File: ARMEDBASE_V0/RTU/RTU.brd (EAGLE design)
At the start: 160 x 100 mm, 25 parts, among them IC1 REG1117, IC2 MEGA8-P, Q1 20Mhz, Q2 2N3904

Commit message: 7805
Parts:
- moved S2 20.5 mm to (5.08, 76.2)
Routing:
- net N$24: track 41.4 -> 74.2 mm, vias 1 -> 0
- net VCC12V: track 41.4 -> 11.7 mm
- net VCC5V: track 129.9 -> 158.8 mm, vias 1 -> 2
- net GND: track 156.7 -> 173.1 mm
- net N$13: track 29.2 -> 16.4 mm
- net N$8: track 46.5 -> 51.1 mm, vias 1 -> 0
- net N$4: track 25.5 -> 24.1 mm
- net RX: track 53.8 -> 53.1 mm

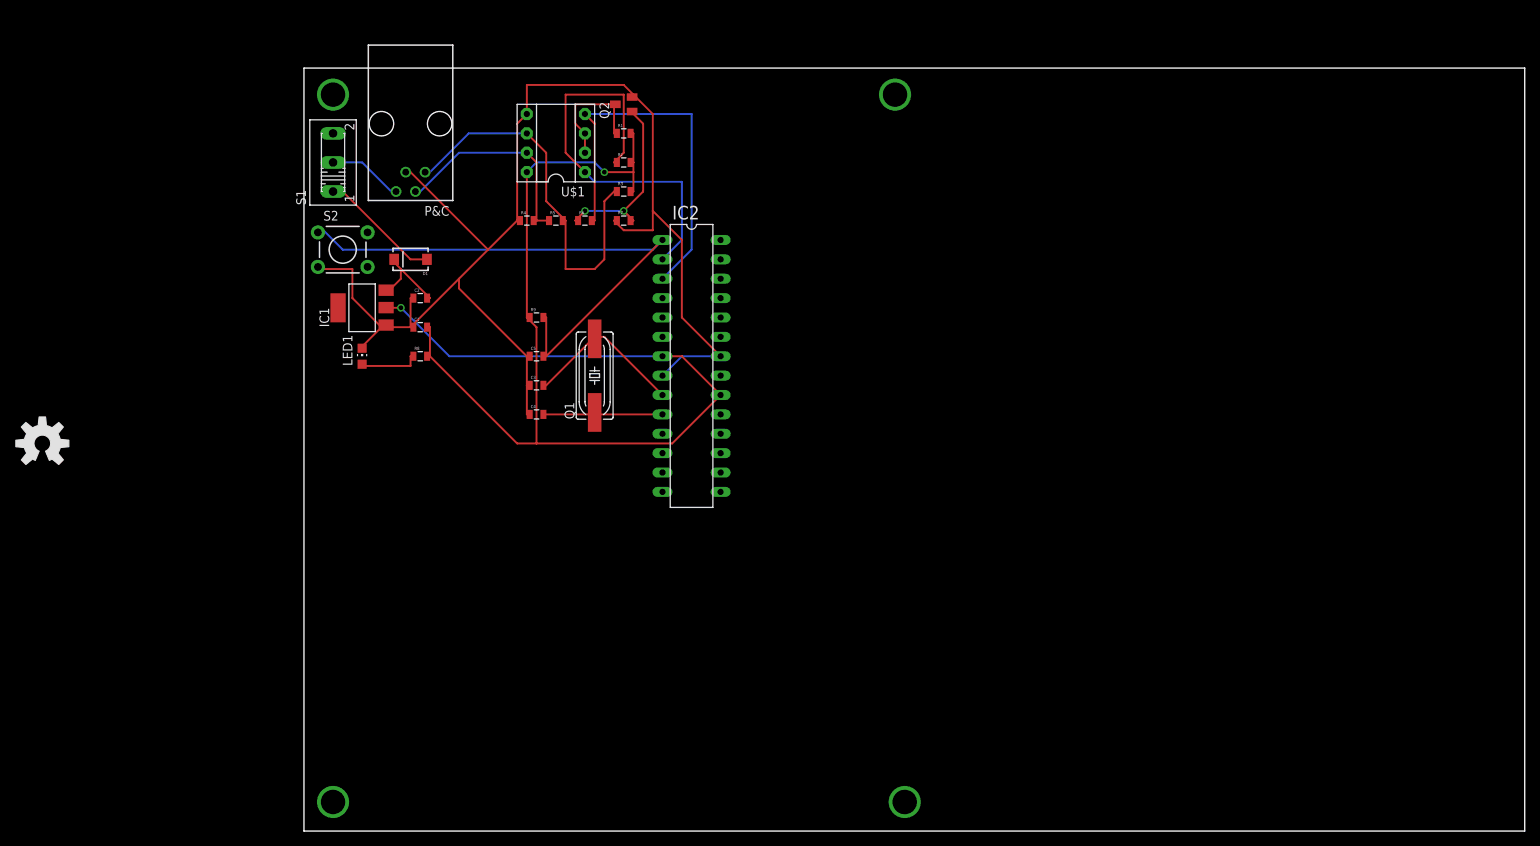
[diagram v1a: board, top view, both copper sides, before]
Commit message: modbus in-out
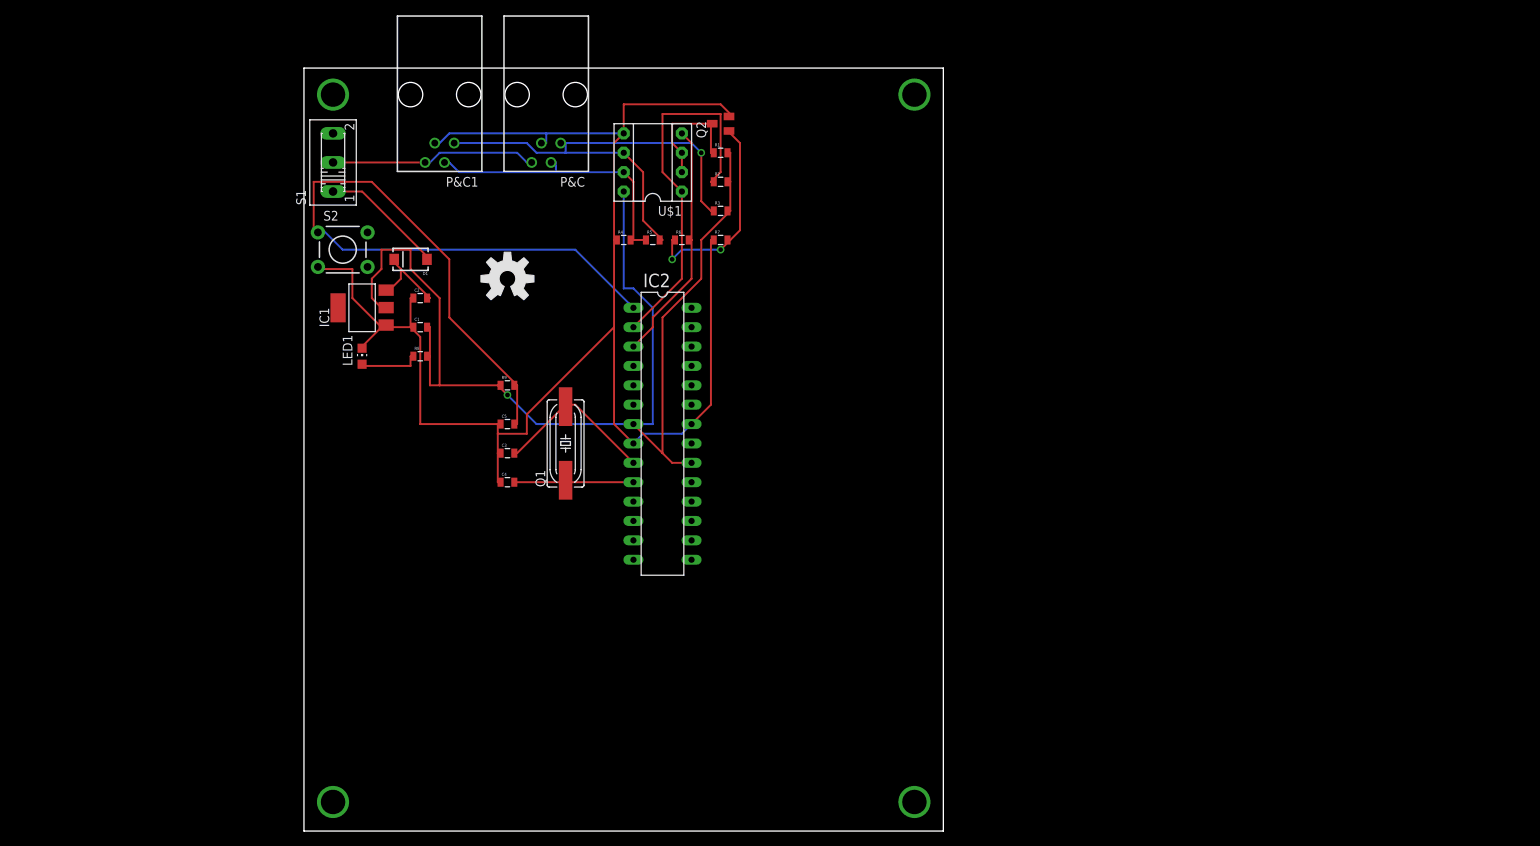
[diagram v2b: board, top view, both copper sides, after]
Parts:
- added P&C1: 14867, con-4ucon:14867
- moved LOGO1 64.7 mm to (26.7, 72.4)
- moved P&C 18.2 mm to (31.8, 96.5)
- moved Q2 13.0 mm to (54.6, 92.7)
- moved R6 13.0 mm to (49.5, 77.5)
- moved R7 13.0 mm to (54.6, 77.5)
- moved R1 13.0 mm to (54.6, 88.9)
- moved R2 13.0 mm to (54.6, 85.1)
- moved R3 13.0 mm to (54.6, 81.3)
- moved R4 13.0 mm to (41.9, 77.5)
- moved R5 13.0 mm to (45.7, 77.5)
- moved U$1 13.0 mm to (45.7, 87.6)
- moved C3 9.67 mm to (26.7, 49.5)
- moved C4 9.67 mm to (26.7, 45.7)
- moved Q1 9.67 mm to (34.3, 50.8)
- moved R9 9.67 mm to (26.7, 58.4)
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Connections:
- net GND: now also P&C1.3
- net N$7: now also P&C1.2
- net N$8: now also P&C1.1
- net VCC: now also P&C1.4
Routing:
- net GND: track 173.1 -> 203.4 mm
- net N$24: track 74.2 -> 100.6 mm
- net TX: track 52.0 -> 32.0 mm
- net VCC: track 9.83 -> 27.1 mm
- net N$8: track 51.1 -> 65.4 mm, vias 0 -> 1
- net N$7: track 28.1 -> 37.4 mm
- net RX: track 53.1 -> 49.0 mm
- net N$4: track 24.1 -> 27.3 mm
- net VCC5V: track 158.8 -> 159.2 mm, vias 2 -> 1
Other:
- board size 160 x 100 mm -> 83.8 x 100 mm

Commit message: arg
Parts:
- moved R9 13.1 mm to (20.3, 69.8)
- moved LED1 10.2 mm to (17.8, 62.2), turned to 90 degrees
- moved R8 6.35 mm to (20.3, 66.0), turned to 180 degrees
- moved Q2 2.84 mm to (55.9, 95.2)
- moved R4 2.84 mm to (43.2, 80.0)
- moved R5 2.84 mm to (47.0, 80.0)
- moved R7 2.84 mm to (55.9, 80.0)
- moved U$1 2.84 mm to (47.0, 90.2)
- moved R6 2.84 mm to (50.8, 80.0)
- moved R1 2.84 mm to (55.9, 91.4)
- moved R2 2.84 mm to (55.9, 87.6)
- moved R3 2.84 mm to (55.9, 83.8)
- moved D1 2.54 mm to (16.5, 74.9)
- moved S2 1.80 mm to (6.35, 77.5)
- moved S1 1.27 mm to (2.54, 87.6)
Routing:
- net N$24: track 100.6 -> 72.4 mm, vias 0 -> 1
- net GND: track 203.4 -> 218.3 mm
- net VCC5V: track 159.2 -> 148.5 mm, vias 1 -> 0
- net N$8: track 65.4 -> 56.4 mm
- net N$13: track 16.8 -> 20.6 mm
- net TX: track 32.0 -> 35.1 mm
- net RX: track 49.0 -> 52.1 mm
- net N$11: track 8.21 -> 5.45 mm
- net VCC: track 27.1 -> 28.4 mm
- net N$4: track 27.3 -> 26.6 mm
- net VCC12V: track 11.7 -> 11.2 mm

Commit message: rtu org
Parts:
- moved R3 33.4 mm to (22.9, 78.7), turned to 180 degrees
- moved R4 25.5 mm to (17.8, 82.5)
- moved R5 24.3 mm to (22.9, 82.5)
- moved R7 19.8 mm to (41.9, 94.0), turned to 90 degrees
- moved R6 14.9 mm to (45.7, 94.0), turned to 270 degrees
- moved U$1 5.24 mm to (45.7, 85.1)
- moved D1 2.84 mm to (15.2, 77.5), turned to 270 degrees
- moved R1 2.54 mm to (55.9, 88.9)
- moved R2 2.54 mm to (55.9, 85.1)
- moved Q2 1.27 mm to (55.9, 94.0)
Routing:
- net GND: track 218.3 -> 166.8 mm
- net VCC5V: track 148.5 -> 187.0 mm, vias 0 -> 1
- net RX: track 52.1 -> 24.9 mm
- net N$8: track 56.4 -> 38.1 mm, vias 1 -> 0
- net N$24: track 72.4 -> 86.6 mm, vias 1 -> 0
- net N$4: track 26.6 -> 18.1 mm, vias 2 -> 0
- net N$13: track 20.6 -> 14.7 mm
- net N$2: track 16.3 -> 14.6 mm
- net N$7: track 37.8 -> 36.5 mm
- net TX: track 35.1 -> 34.5 mm

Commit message: MCU almost
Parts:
- added F1: 100mA, special:FUSE
- moved IC2 31.8 mm to (38.1, 21.6), turned to 180 degrees
- moved C1 30.5 mm to (15.2, 35.6)
- moved Q2 30.5 mm to (55.9, 63.5)
- moved R1 30.5 mm to (55.9, 58.4)
- moved R2 30.5 mm to (55.9, 54.6)
- moved R6 30.5 mm to (45.7, 63.5)
- moved R7 30.5 mm to (41.9, 63.5)
- moved R8 30.5 mm to (20.3, 35.6)
- moved U$1 30.5 mm to (45.7, 54.6)
- moved C2 30.5 mm to (15.2, 39.4)
- moved D1 30.5 mm to (15.2, 47.0)
- moved IC1 30.5 mm to (7.62, 38.1)
- moved LED1 30.5 mm to (17.8, 31.8)
- moved R3 30.5 mm to (22.9, 48.3)
- moved R4 30.5 mm to (17.8, 52.1)
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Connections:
- new net N$9: C1.2, F1.1, IC1.2, R8.2
- net VCC5V: now also F1.2; no longer C1.2, IC1.2, R8.2
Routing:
- net VCC5V: track 187.0 -> 134.9 mm
- net N$21: track 21.7 -> 60.1 mm
- net N$9: track 0.00 -> 31.9 mm
- net N$24: track 86.6 -> 99.3 mm, vias 0 -> 1
- net RX: track 24.9 -> 33.0 mm
- net N$23: track 15.9 -> 22.0 mm
- net TX: track 34.5 -> 40.6 mm
- net GND: track 166.8 -> 164.2 mm
- net N$8: track 38.1 -> 39.2 mm
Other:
- board size 83.8 x 100 mm -> 99 x 69.5 mm

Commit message: rtu fuse
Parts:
- F1: value 100mA -> 100ma; device special:FUSE -> _hhn_PtcFuses_Siba_r500_Ozan:1820
- moved F1 6.35 mm to (6.35, 26.7), turned to 180 degrees
- moved IC1 2.84 mm to (6.35, 35.6), turned to 180 degrees
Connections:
- net N$9: now also F1.2, IC1.3; no longer C1.2, F1.1, IC1.2, R8.2
- net VCC12V: now also F1.1; no longer IC1.3
- net VCC5V: now also C1.2, IC1.2, R8.2; no longer F1.2
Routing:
- net N$9: track 31.9 -> 12.1 mm
- net N$21: track 60.1 -> 42.6 mm
- net N$24: track 99.3 -> 85.6 mm
- net VCC12V: track 10.9 -> 23.9 mm
- net GND: track 164.2 -> 153.1 mm
- net N$4: track 18.1 -> 21.4 mm
- net VCC5V: track 134.9 -> 132.9 mm
- net N$7: track 36.5 -> 35.2 mm
- net N$8: track 39.2 -> 38.0 mm
- net N$23: track 22.0 -> 21.2 mm
